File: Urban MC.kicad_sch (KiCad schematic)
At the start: 74 parts, among them J1 Conn_01x02, J2 Conn_01x02, J3 Conn_01x03, J4 Conn_01x02, Q1 IQE022N06LM5CGSCATMA1, Q10 IQE022N06LM5CGSCATMA1, Q11 IQE022N06LM5CGSCATMA1, Q12 IQE022N06LM5CGSCATMA1, Q13 IQE022N06LM5CGSCATMA1, Q14 IQE022N06LM5CGSCATMA1, Q15 IQE022N06LM5CGSCATMA1, Q16 IQE022N06LM5CGSCATMA1, Q17 IQE022N06LM5CGSCATMA1, Q18 IQE022N06LM5CGSCATMA1, Q19 IQE022N06LM5CGSCATMA1, Q2 IQE022N06LM5CGSCATMA1, Q20 IQE022N06LM5CGSCATMA1, Q21 IQE022N06LM5CGSCATMA1, Q22 IQE022N06LM5CGSCATMA1, Q23 IQE022N06LM5CGSCATMA1, Q24 IQE022N06LM5CGSCATMA1, Q3 IQE022N06LM5CGSCATMA1, Q4 IQE022N06LM5CGSCATMA1, Q5 IQE022N06LM5CGSCATMA1, Q6 IQE022N06LM5CGSCATMA1, Q7 IQE022N06LM5CGSCATMA1, Q8 IQE022N06LM5CGSCATMA1, Q9 IQE022N06LM5CGSCATMA1, SW1 CAN_TERM, SW2 SW_Push, U1 MCP2561/2, U1 MCP4725, U2 MCP2515-xSO, Y1 8MHz

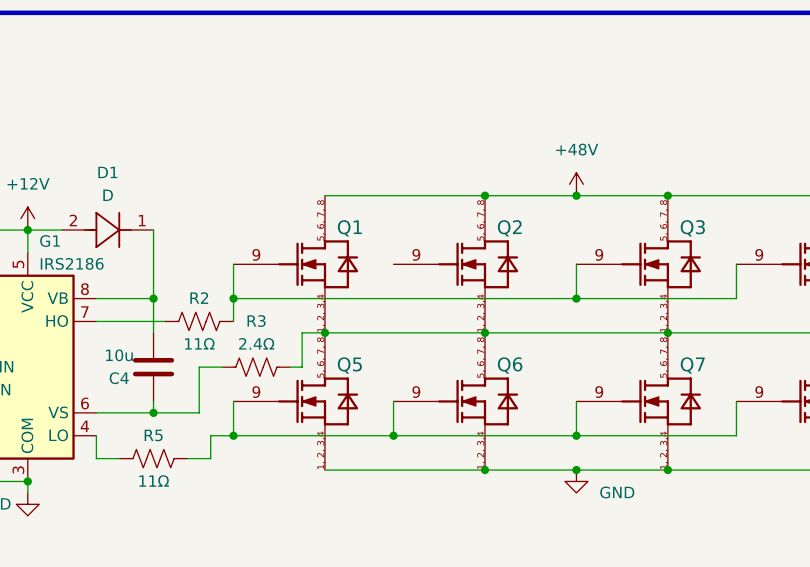
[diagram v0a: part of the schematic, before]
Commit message: MOSFETsection with some changes
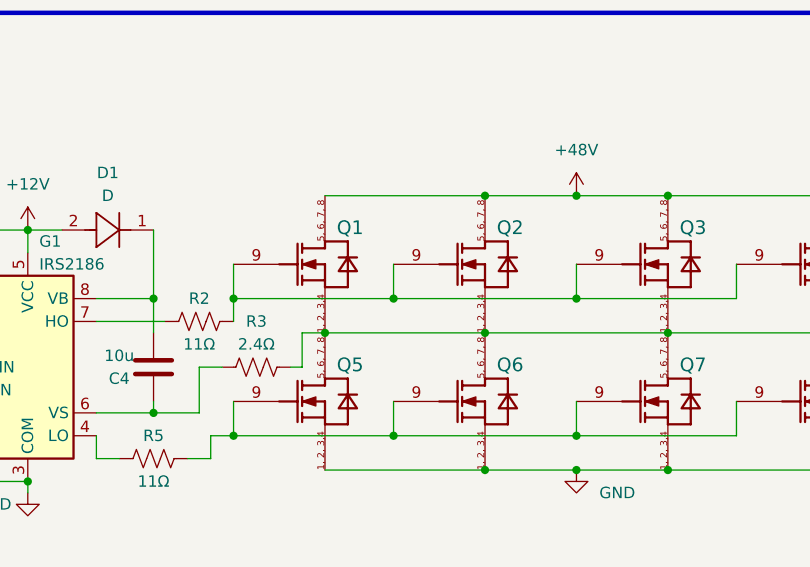
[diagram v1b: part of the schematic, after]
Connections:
- net at Q1.9 (GATE), Q3.9 (GATE), Q4.9 (GATE)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: now also Q2.9 (GATE)
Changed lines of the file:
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@@
+	)
+	(junction
+		(at 335.28 64.77)
+		(diameter 0)
+		(color 0 0 0 0)
 	)
 	(junction
@@
 	(wire
 		(pts
+			(xy 335.28 60.96) (xy 335.28 64.77)
+		)
+		(stroke
+			(width 0)
+			(type default)
+		)
+	)
+	(wire
+		(pts
 			(xy 327.66 83.82) (xy 345.44 83.82)
 		)
@@
 	(wire
 		(pts
-			(xy 317.5 64.77) (xy 355.6 64.77)
+			(xy 317.5 64.77) (xy 335.28 64.77)
 		)
 		(stroke
@@
 		)
 		(stroke
+			(width 0)
+			(type default)
+		)
+	)
+	(wire
+		(pts
+			(xy 335.28 64.77) (xy 355.6 64.77)
+		)
+		(stroke

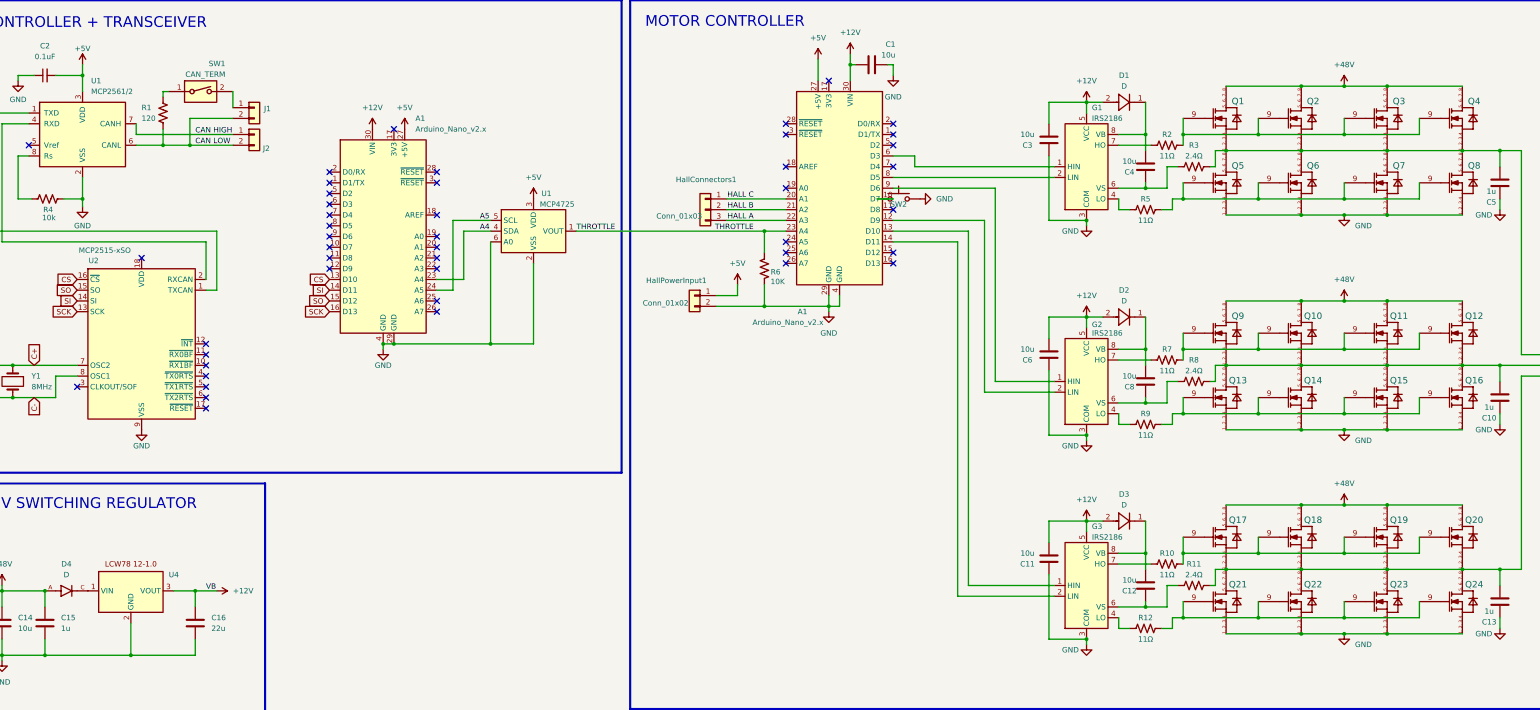
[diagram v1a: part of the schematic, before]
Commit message: symbol changes and filled zone solution, still looking for more feedback
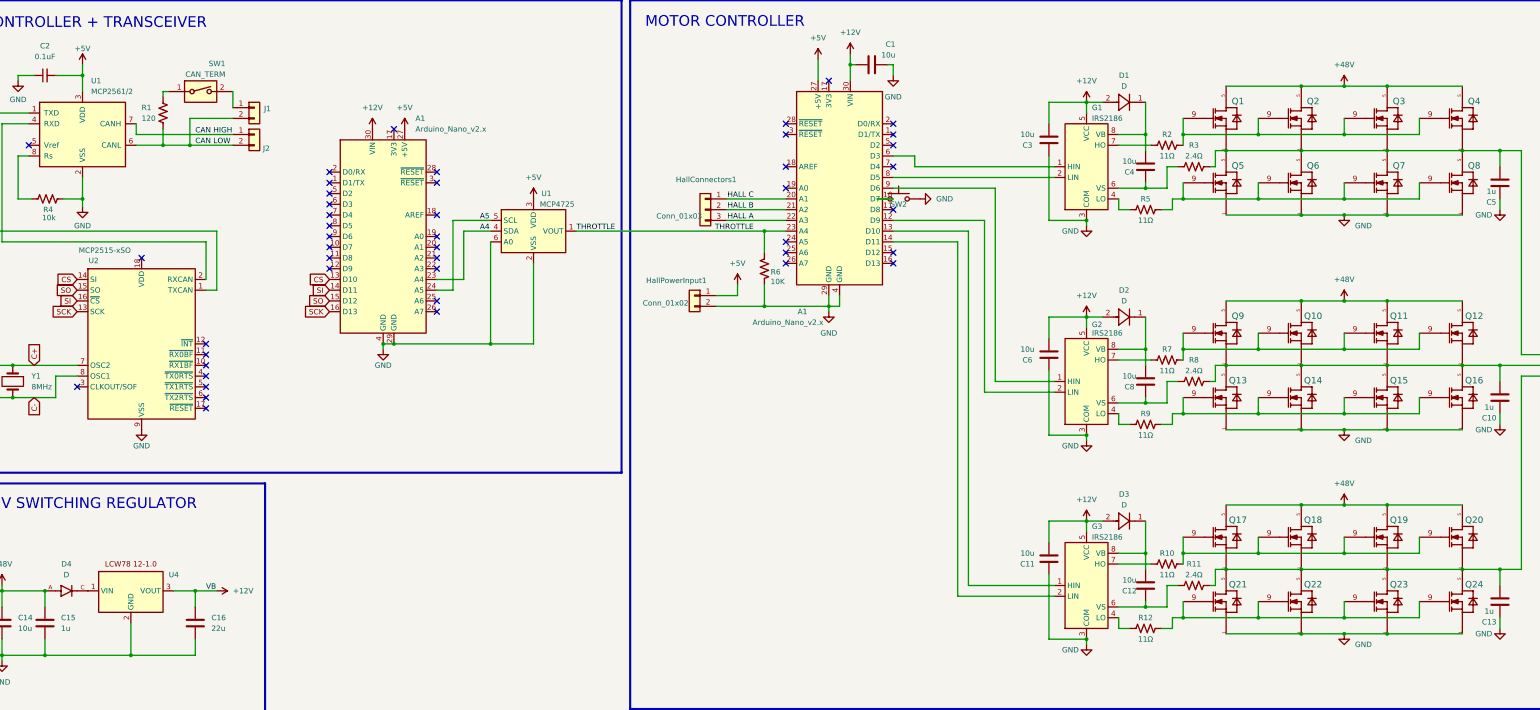
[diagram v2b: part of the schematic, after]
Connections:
- net CS: now also U2.14 (SI); no longer U2.16 (~{CS})
- net SI: now also U2.16 (~{CS}); no longer U2.14 (SI)
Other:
- moved on the sheet: Q1, Q10, Q11, Q12, Q13, Q14, Q15, Q16, Q17, Q18, Q19, Q2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

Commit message: in the middle of layout changes- expanding right side and drawing gate driver traces
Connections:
- net at C5.2, Q1.1 (SOURCE1), Q1.2 (SOURCE2)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: now also J3.3 (Pin_3); no longer J3.1 (Pin_1)
- net at C13.2, Q17.1 (SOURCE1), Q17.2 (SOURCE2)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: now also J3.1 (Pin_1); no longer J3.3 (Pin_3)
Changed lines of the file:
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@@
+	)
+	(junction
+		(at 392.43 119.38)
+		(diameter 0)
+		(color 0 0 0 0)
 	)
 	(junction
@@
 	)
 	(junction
-		(at 392.43 119.38)
-		(diameter 0)
-		(color 0 0 0 0)
-	)
-	(junction
 		(at 383.54 119.38)
 		(diameter 0)
@@
 	(wire
 		(pts
-			(xy 397.51 121.92) (xy 410.21 121.92)
-		)
-		(stroke
-			(width 0)
-			(type default)
-		)
-	)
-	(wire
-		(pts
 			(xy 317.5 115.57) (xy 317.5 111.76)
 		)
@@
 	(wire
 		(pts
+			(xy 402.59 116.84) (xy 410.21 116.84)
+		)
+		(stroke
+			(width 0)
+			(type default)
+		)
+	)
+	(wire
+		(pts
 			(xy 83.82 172.72) (xy 88.9 172.72)
 		)
@@
 	(wire
 		(pts
+			(xy 405.13 113.03) (xy 405.13 121.92)
+		)
+		(stroke
+			(width 0)
+			(type default)
+		)
+	)
+	(wire
+		(pts
 			(xy 302.26 181.61) (xy 302.26 179.07)
 		)
@@
 	(wire
 		(pts
+			(xy 392.43 119.38) (xy 410.21 119.38)
+		)
+		(stroke
+			(width 0)
+			(type default)
+		)
+	)
+	(wire
+		(pts
 			(xy 238.76 45.72) (xy 238.76 48.26)
 		)
@@
 	(wire
 		(pts
-			(xy 392.43 119.38) (xy 410.21 119.38)
-		)
-		(stroke
-			(width 0)
-			(type default)
-		)
-	)
-	(wire
-		(pts
 			(xy 218.44 105.41) (xy 233.68 105.41)
 		)
@@
 	(wire
 		(pts
+			(xy 392.43 64.77) (xy 392.43 68.58)
+		)
+		(stroke
+			(width 0)
+			(type default)
+		)
+	)
+	(wire
+		(pts
 			(xy 212.09 102.87) (xy 212.09 100.33)
 		)
@@
 	(wire
 		(pts
-			(xy 397.51 116.84) (xy 410.21 116.84)
-		)
-		(stroke
-			(width 0)
-			(type default)
-		)
-	)
-	(wire
-		(pts
 			(xy 308.61 107.95) (xy 308.61 115.57)
 		)
@@
 	(wire
 		(pts
+			(xy 402.59 121.92) (xy 402.59 116.84)
+		)
+		(stroke
+			(width 0)
+			(type default)
+		)
+	)
+	(wire
+		(pts
 			(xy 294.64 185.42) (xy 294.64 184.15)
 		)
@@
 	(wire
 		(pts
-			(xy 392.43 68.58) (xy 397.51 68.58)
+			(xy 392.43 64.77) (xy 397.51 64.77)
 		)
 		(stroke
@@
 	(wire
 		(pts
-			(xy 397.51 68.58) (xy 397.51 116.84)
+			(xy 397.51 64.77) (xy 397.51 113.03)
 		)
 		(stroke
@@
 	(wire
 		(pts
+			(xy 405.13 121.92) (xy 410.21 121.92)
+		)
+		(stroke
+			(width 0)
+			(type default)
+		)
+	)
+	(wire
+		(pts
 			(xy 38.1 187.96) (xy 38.1 189.23)
 		)
@@
 	(wire
 		(pts
+			(xy 397.51 121.92) (xy 402.59 121.92)
+		)
+		(stroke
+			(width 0)
+			(type default)
+		)
+	)
+	(wire
+		(pts
 			(xy 247.65 48.26) (xy 248.92 48.26)
 		)
@@
 		)
 		(stroke
+			(width 0)
+			(type default)
+		)
+	)
+	(wire
+		(pts
+			(xy 397.51 113.03) (xy 405.13 113.03)
+		)
+		(stroke

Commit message: grounding components with vias instead of long traces, 5V filled zone and MCP4725 complementary components
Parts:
- added C17: 0.1uF, Capacitor_SMD:C_0805_2012Metric_Pad1.18x1.45mm_HandSolder, symbol Device:C_Small
- added C18: 10uF, Capacitor_SMD:C_0805_2012Metric_Pad1.18x1.45mm_HandSolder, symbol Device:C_Small
- added R13, R14: 10K, Resistor_SMD:R_0402_1005Metric, symbol Device:R_US
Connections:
- net +5V: now also C17.1, C18.1, R13.1, R14.1
- net A4: now also R14.2
- net A5: now also R13.2
- net GND: now also C17.2, C18.2

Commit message: Phase output net names, keepouts on mounting holes, logo, other small fixes
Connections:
- net +12V: no longer A1.30 (VIN), C1.1
- net +5V: now also A1.30 (VIN), C1.1, U2.18 (VDD)
- net PHASE 1 OUTPUT: now reaches C5.2, J3.3 (Pin_3), Q1.1 (SOURCE1), Q1.2 (SOURCE2), Q1.3 (SOURCE3), Q1.4 (SOURCE4), Q2.1 (SOURCE1), Q2.2 (SOURCE2), Q2.3 (SOURCE3), Q2.4 (SOURCE4), Q3.1 (SOURCE1), Q3.2 (SOURCE2), Q3.3 (SOURCE3), Q3.4 (SOURCE4), Q4.1 (SOURCE1), Q4.2 (SOURCE2), Q4.3 (SOURCE3), Q4.4 (SOURCE4), Q5.5 (DRAIN1), Q5.6 (DRAIN2), Q5.7 (DRAIN3), Q5.8 (DRAIN4), Q6.5 (DRAIN1), Q6.6 (DRAIN2), Q6.7 (DRAIN3), Q6.8 (DRAIN4), Q7.5 (DRAIN1), Q7.6 (DRAIN2), Q7.7 (DRAIN3), Q7.8 (DRAIN4), Q8.5 (DRAIN1), Q8.6 (DRAIN2), Q8.7 (DRAIN3), Q8.8 (DRAIN4), R3.2
- net PHASE 3 OUTPUT: now reaches C13.2, J3.1 (Pin_1), Q17.1 (SOURCE1), Q17.2 (SOURCE2), Q17.3 (SOURCE3), Q17.4 (SOURCE4), Q18.1 (SOURCE1), Q18.2 (SOURCE2), Q18.3 (SOURCE3), Q18.4 (SOURCE4), Q19.1 (SOURCE1), Q19.2 (SOURCE2), Q19.3 (SOURCE3), Q19.4 (SOURCE4), Q20.1 (SOURCE1), Q20.2 (SOURCE2), Q20.3 (SOURCE3), Q20.4 (SOURCE4), Q21.5 (DRAIN1), Q21.6 (DRAIN2), Q21.7 (DRAIN3), Q21.8 (DRAIN4), Q22.5 (DRAIN1), Q22.6 (DRAIN2), Q22.7 (DRAIN3), Q22.8 (DRAIN4), Q23.5 (DRAIN1), Q23.6 (DRAIN2), Q23.7 (DRAIN3), Q23.8 (DRAIN4), Q24.5 (DRAIN1), Q24.6 (DRAIN2), Q24.7 (DRAIN3), Q24.8 (DRAIN4), R11.2
- net PHASE 2 OUTPUT: now reaches C10.2, J3.2 (Pin_2), Q10.1 (SOURCE1), Q10.2 (SOURCE2), Q10.3 (SOURCE3), Q10.4 (SOURCE4), Q11.1 (SOURCE1), Q11.2 (SOURCE2), Q11.3 (SOURCE3), Q11.4 (SOURCE4), Q12.1 (SOURCE1), Q12.2 (SOURCE2), Q12.3 (SOURCE3), Q12.4 (SOURCE4), Q13.5 (DRAIN1), Q13.6 (DRAIN2), Q13.7 (DRAIN3), Q13.8 (DRAIN4), Q14.5 (DRAIN1), Q14.6 (DRAIN2), Q14.7 (DRAIN3), Q14.8 (DRAIN4), Q15.5 (DRAIN1), Q15.6 (DRAIN2), Q15.7 (DRAIN3), Q15.8 (DRAIN4), Q16.5 (DRAIN1), Q16.6 (DRAIN2), Q16.7 (DRAIN3), Q16.8 (DRAIN4), Q9.1 (SOURCE1), Q9.2 (SOURCE2), Q9.3 (SOURCE3), Q9.4 (SOURCE4), R8.2
- no-connect marks 45 -> 44
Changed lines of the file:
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@@
 	)
 	(no_connect
-		(at 71.12 93.98)
-	)
-	(no_connect
 		(at 140.97 76.2)
 	)
@@
 	(wire
 		(pts
+			(xy 365.76 119.38) (xy 345.44 119.38)
+		)
+		(stroke
+			(width 0)
+			(type default)
+		)
+	)
+	(wire
+		(pts
 			(xy 308.61 64.77) (xy 308.61 68.58)
 		)
@@
 	(wire
 		(pts
-			(xy 345.44 119.38) (xy 365.76 119.38)
-		)
-		(stroke
-			(width 0)
-			(type default)
-		)
-	)
-	(wire
-		(pts
 			(xy 92.71 60.96) (xy 82.55 60.96)
 		)
@@
 	(wire
 		(pts
+			(xy 397.51 68.58) (xy 392.43 68.58)
+		)
+		(stroke
+			(width 0)
+			(type default)
+		)
+	)
+	(wire
+		(pts
 			(xy 313.69 123.19) (xy 313.69 128.27)
 		)
@@
 	(wire
 		(pts
-			(xy 392.43 64.77) (xy 392.43 68.58)
-		)
-		(stroke
-			(width 0)
-			(type default)
-		)
-	)
-	(wire
-		(pts
 			(xy 212.09 102.87) (xy 212.09 100.33)
 		)
@@
 	(wire
 		(pts
+			(xy 365.76 68.58) (xy 345.44 68.58)
+		)
+		(stroke
+			(width 0)
+			(type default)
+		)
+	)
+	(wire
+		(pts
 			(xy 308.61 77.47) (xy 302.26 77.47)
 		)
@@
 	(wire
 		(pts
-			(xy 392.43 64.77) (xy 397.51 64.77)
-		)
-		(stroke
-			(width 0)
-			(type default)
-		)
-	)
-	(wire
-		(pts
 			(xy 35.56 170.18) (xy 35.56 172.72)
 		)
@@
 	(wire
 		(pts
-			(xy 397.51 64.77) (xy 397.51 113.03)
+			(xy 397.51 68.58) (xy 397.51 113.03)
 		)
 		(stroke
@@
 	(wire
 		(pts
-			(xy 345.44 68.58) (xy 365.76 68.58)
-		)
-		(stroke
-			(width 0)
-			(type default)
-		)
-	)
-	(wire
-		(pts
 			(xy 38.1 62.23) (xy 44.45 62.23)
 		)
@@
 		)
 	)
+	(label "PHASE 3 OUTPUT"
+		(at 397.51 167.64 0)
+		(fields_autoplaced yes)
+		(effects
+			(font
+				(size 1.27 1.27)
+			)
+			(justify left bottom)
+		)
+	)
 	(label "HALL C"
 		(at 215.9 80.01 180)
@@
 		)
 	)
+	(label "PHASE 1 OUTPUT"
+		(at 397.51 68.58 0)
+		(fields_autoplaced yes)
+		(effects
+			(font
+				(size 1.27 1.27)
+			)
+			(justify left bottom)
+		)
+	)
 	(label "CAN HIGH"
 		(at 83.82 64.77 0)
@@
 		)
 	)
+	(label "PHASE 2 OUTPUT"
+		(at 383.54 119.38 0)
+		(fields_autoplaced yes)
+		(effects
+			(font
+				(size 1.27 1.27)
+			)
+			(justify left bottom)
+		)
+	)
 	(label "VB"
 		(at 86.36 172.72 0)
@@
 			)
 		)
-		(property "Datasheet" "~"
+		(property "Datasheet" "https://product.tdk.com/en/system/files/dam/doc/product/capacitor/ceramic/mlcc/catalog/mlcc_commercial_midvoltage_en.pdf"
 			(at 392.43 175.26 0)
 			(effects
@@
 			)
 		)
-		(property "Datasheet" "~"
+		(property "Datasheet" "https://product.tdk.com/en/system/files/dam/doc/product/capacitor/ceramic/mlcc/catalog/mlcc_commercial_midvoltage_en.pdf"
 			(at 392.43 127 0)
 			(effects
@@
 			)
 		)
-		(property "Datasheet" "~"
+		(property "Datasheet" "https://product.tdk.com/en/system/files/dam/doc/product/capacitor/ceramic/mlcc/catalog/mlcc_commercial_midvoltage_en.pdf"
 			(at 392.43 76.2 0)
 			(effects
@@
 	)
 	(symbol
+		(lib_id "power:+5V")
+		(at 238.76 45.72 0)
+		(unit 1)
+		(exclude_from_sim no)
+		(in_bom yes)
+		(on_board yes)
+		(dnp no)
+		(property "Reference" "#PWR01"
+			(at 238.76 49.53 0)
+			(effects
+				(font
+					(size 1.27 1.27)
+				)
+				(hide yes)
+			)
+		)
+		(property "Value" "+5V"
+			(at 238.76 40.64 0)
+			(effects
+				(font
+					(size 1.27 1.27)
+				)
+			)
+		)
+		(property "Footprint" ""
+			(at 238.76 45.72 0)
+			(effects
+				(font
+					(size 1.27 1.27)
+				)
+				(hide yes)
+			)
+		)
+		(property "Datasheet" ""
+			(at 238.76 45.72 0)
+			(effects
+				(font
+					(size 1.27 1.27)
+				)
+				(hide yes)
+			)
+		)
+		(property "Description" "Power symbol creates a global label with name \"+5V\""
+			(at 238.76 45.72 0)
+			(effects
+				(font
+					(size 1.27 1.27)
+				)
+				(hide yes)
+			)
+		)
+		(pin "1"
+		)
+		(instances
+			(project "Urban MC"
+				(path "/9c188f5e-4c43-43bc-b719-7c7a34d1ae77"
+					(reference "#PWR01")
+					(unit 1)
+				)
+			)
+		)
+	)
+	(symbol
 		(lib_name "root_0_IQE022N06LM5CGSC_5")
 		(lib_id "Supermileage Symbols:root_0_IQE022N06LM5CGSC")
@@
 	)
 	(symbol
-		(lib_name "root_0_IQE022N06LM5CGSC_5")
-		(lib_id "Supermileage Symbols:root_0_IQE022N06LM5CGSC")
-		(at 378.46 157.48 0)
+		(lib_id "power:+5V")
+		(at 71.12 93.98 0)
 		(unit 1)
 		(exclude_from_sim no)
@@
 		(on_board yes)
 		(dnp no)
-		(property "Reference" "Q20"
-			(at 386.334 155.956 0)
+		(property "Reference" "#PWR037"
+			(at 71.12 97.79 0)
 			(effects
 				(font
-					(size 1.524 1.524)
+					(size 1.27 1.27)
 				)
+				(hide yes)
 			)
 		)
-		(property "Value" "IQE022N06LM5CGSCATMA1"
-			(at 394.716 149.606 0)
+		(property "Value" "+5V"
+			(at 71.12 88.9 0)
 			(effects
 				(font
-					(size 1.524 1.524)
+					(size 1.27 1.27)
 				)
-				(hide yes)
 			)
 		)
-		(property "Footprint" "urban_mc_custom_footprints:IFX-PG-WHTFN-9-1-V"
-			(at 378.46 157.48 0)
+		(property "Footprint" ""
+			(at 71.12 93.98 0)
 			(effects
 				(font
@@
 			)
 		)
-		(property "Datasheet" "https://www.infineon.com/dgdl/Infineon-IQE022N06LM5CGSC-DataSheet-v02_00-EN.pdf?fileId=8ac78c8c85ecb34701866d7ad6fd51c1"
-			(at 378.46 157.48 0)
+		(property "Datasheet" ""
+			(at 71.12 93.98 0)
 			(effects
 				(font
@@
 			)
 		)
-		(property "Description" "Insulated-Gate Field-Effect Transistor (IGFET), N-Channel, Enhancement, Body Diode, Pin 1 Source, 2 Source, 3 Source, 4 Sourse, 5 Drain, 6 Drain, 7 Drain, 8 Drain, 9 Gate, 9 Pins"
-			(at 378.46 157.48 0)
+		(property "Description" "Power symbol creates a global label with name \"+5V\""
+			(at 71.12 93.98 0)
 			(effects
 				(font
@@
 		(pin "1"
 		)
-		(pin "5"
-		)
-		(pin "3"
-		)
-		(pin "9"
-		)
-		(pin "6"
-		)
-		(pin "8"
-		)
-		(pin "4"
-		)
-		(pin "2"
-		)
-		(pin "7"
-		)
 		(instances
 			(project "Urban MC"
 				(path "/9c188f5e-4c43-43bc-b719-7c7a34d1ae77"
-					(reference "Q20")
+					(reference "#PWR037")
 					(unit 1)
 				)
@@
 	)
 	(symbol
-		(lib_id "power:+12V")
-		(at 238.76 45.72 0)
+		(lib_name "root_0_IQE022N06LM5CGSC_5")
+		(lib_id "Supermileage Symbols:root_0_IQE022N06LM5CGSC")
+		(at 378.46 157.48 0)
 		(unit 1)
 		(exclude_from_sim no)
@@
 		(on_board yes)
 		(dnp no)
-		(fields_autoplaced yes)
-		(property "Reference" "#PWR01"
-			(at 238.76 49.53 0)
+		(property "Reference" "Q20"
+			(at 386.334 155.956 0)
 			(effects
 				(font
-					(size 1.27 1.27)
+					(size 1.524 1.524)
 				)
-				(hide yes)
 			)
 		)
-		(property "Value" "+12V"
-			(at 238.76 40.64 0)
+		(property "Value" "IQE022N06LM5CGSCATMA1"
+			(at 394.716 149.606 0)
 			(effects
 				(font
-					(size 1.27 1.27)
+					(size 1.524 1.524)
 				)
+				(hide yes)
 			)
 		)
-		(property "Footprint" ""
-			(at 238.76 45.72 0)
+		(property "Footprint" "urban_mc_custom_footprints:IFX-PG-WHTFN-9-1-V"
+			(at 378.46 157.48 0)
 			(effects
 				(font
@@
 			)
 		)
-		(property "Datasheet" ""
-			(at 238.76 45.72 0)
+		(property "Datasheet" "https://www.infineon.com/dgdl/Infineon-IQE022N06LM5CGSC-DataSheet-v02_00-EN.pdf?fileId=8ac78c8c85ecb34701866d7ad6fd51c1"
+			(at 378.46 157.48 0)
 			(effects
 				(font
@@
 			)
 		)
-		(property "Description" "Power symbol creates a global label with name \"+12V\""
-			(at 238.76 45.72 0)
+		(property "Description" "Insulated-Gate Field-Effect Transistor (IGFET), N-Channel, Enhancement, Body Diode, Pin 1 Source, 2 Source, 3 Source, 4 Sourse, 5 Drain, 6 Drain, 7 Drain, 8 Drain, 9 Gate, 9 Pins"
+			(at 378.46 157.48 0)
 			(effects
 				(font
@@
 		(pin "1"
 		)
+		(pin "5"
+		)
+		(pin "3"
+		)
+		(pin "9"
+		)
+		(pin "6"
+		)
+		(pin "8"
+		)
+		(pin "4"
+		)
+		(pin "2"
+		)
+		(pin "7"
+		)
 		(instances
-			(project ""
+			(project "Urban MC"
 				(path "/9c188f5e-4c43-43bc-b719-7c7a34d1ae77"
-					(reference "#PWR01")
+					(reference "Q20")
 					(unit 1)
 				)

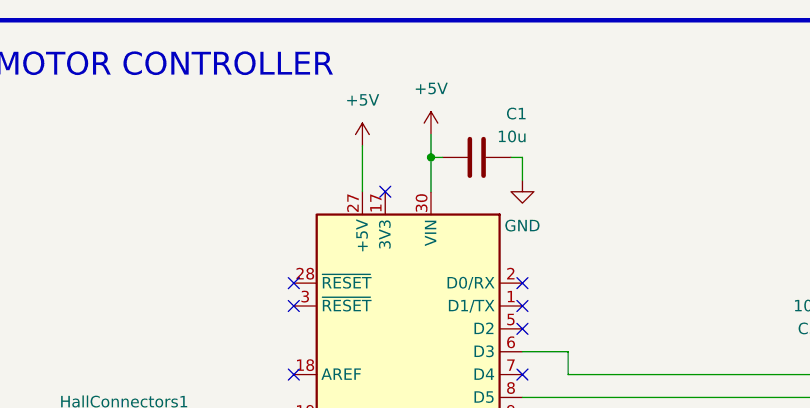
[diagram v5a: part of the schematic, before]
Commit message: 5V filled zone edits
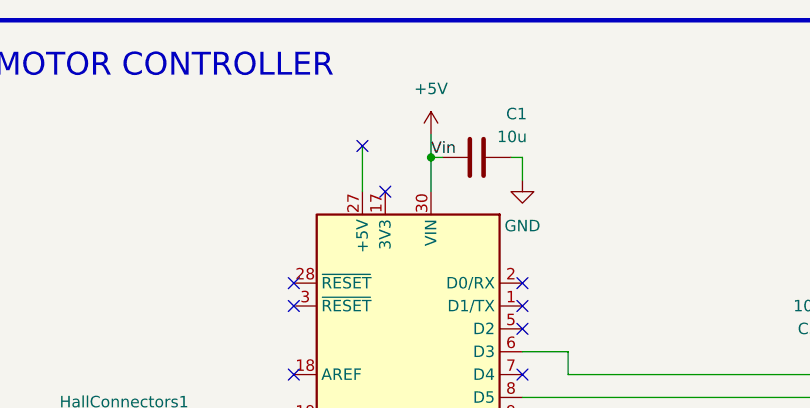
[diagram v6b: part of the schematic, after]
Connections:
- net +5V: no longer A1.27 (+5V)
- no-connect marks 44 -> 45
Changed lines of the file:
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@@
 	)
 	(no_connect
+		(at 231.14 46.99)
+	)
+	(no_connect
 		(at 86.36 124.46)
 	)
@@
 		)
 	)
+	(label "Vin"
+		(at 238.76 48.26 0)
+		(fields_autoplaced yes)
+		(effects
+			(font
+				(size 1.27 1.27)
+			)
+			(justify left bottom)
+		)
+	)
 	(label "VB"
 		(at 86.36 172.72 0)
@@
 					(unit 1)
 				)
-			)
-		)
-	)
-	(symbol
-		(lib_id "power:+5V")
-		(at 231.14 46.99 0)
-		(unit 1)
-		(exclude_from_sim no)
-		(in_bom yes)
-		(on_board yes)
-		(dnp no)
-		(property "Reference" "#PWR02"
-			(at 231.14 50.8 0)
-			(effects
-				(font
-					(size 1.27 1.27)
-				)
-				(hide yes)
-			)
-		)
-		(property "Value" "+5V"
-			(at 231.14 41.91 0)
-			(effects
-				(font
-					(size 1.27 1.27)
-				)
-			)
-		)
-		(property "Footprint" ""
-			(at 231.14 46.99 0)
-			(effects
-				(font
-					(size 1.27 1.27)
-				)
-				(hide yes)
-			)
-		)
-		(property "Datasheet" ""
-			(at 231.14 46.99 0)
-			(effects
-				(font
-					(size 1.27 1.27)
-				)
-				(hide yes)
-			)
-		)
-		(property "Description" "Power symbol creates a global label with name \"+5V\""
-			(at 231.14 46.99 0)
-			(effects
-				(font
-					(size 1.27 1.27)
-				)
-				(hide yes)
-			)
-		)
-		(pin "1"
-		)
-		(instances
-			(project ""
-				(path "/9c188f5e-4c43-43bc-b719-7c7a34d1ae77"
-					(reference "#PWR02")
-					(unit 1)
-				)
